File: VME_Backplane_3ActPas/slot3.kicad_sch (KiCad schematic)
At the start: 7 parts, among them X101 DIN41612_03x32_ABC_VMEbus, X402A1 Jumper_2_Open, X402B1 Jumper_2_Open, X402C1 Jumper_2_Open, X402D1 Jumper_2_Open, X502 Jumper_2_Open

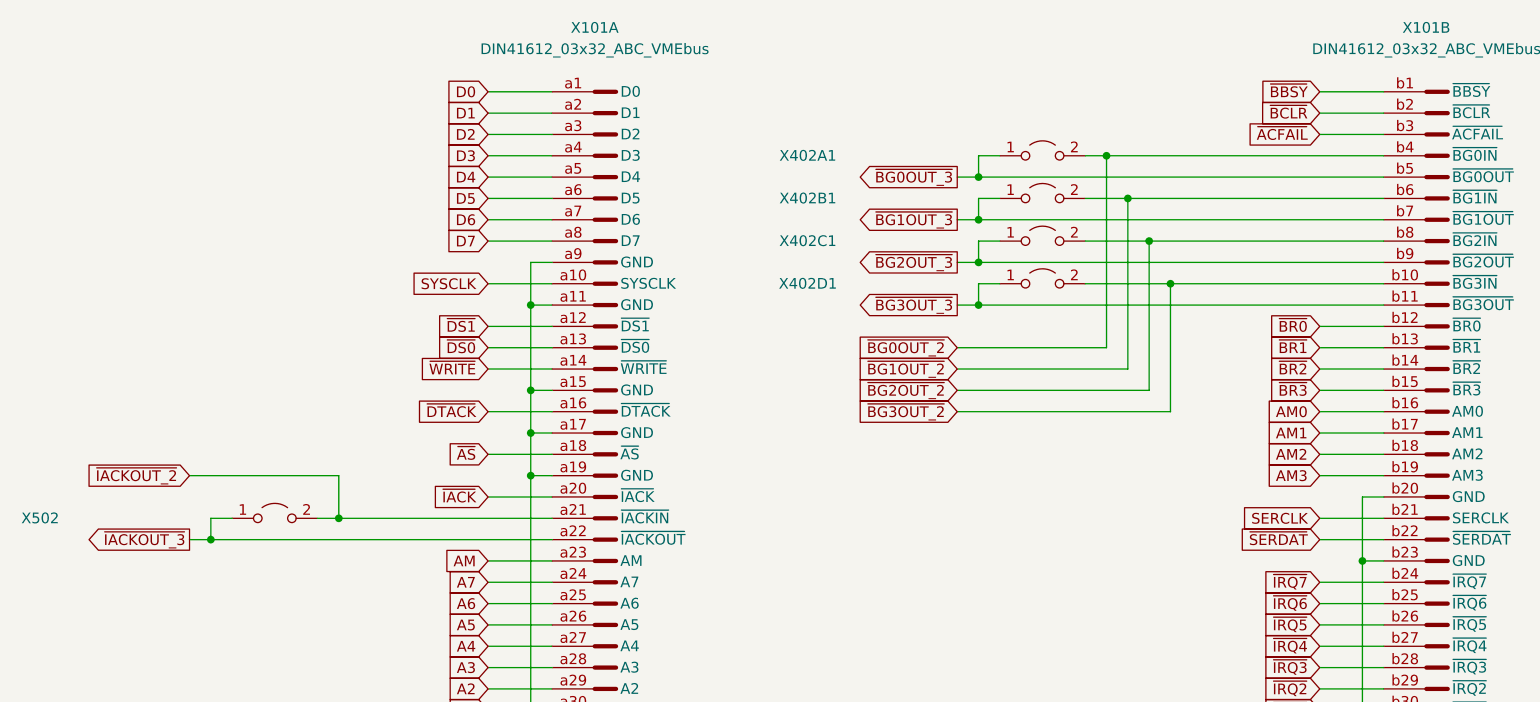
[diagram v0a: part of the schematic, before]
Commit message: Rename sheets to reflect their slots
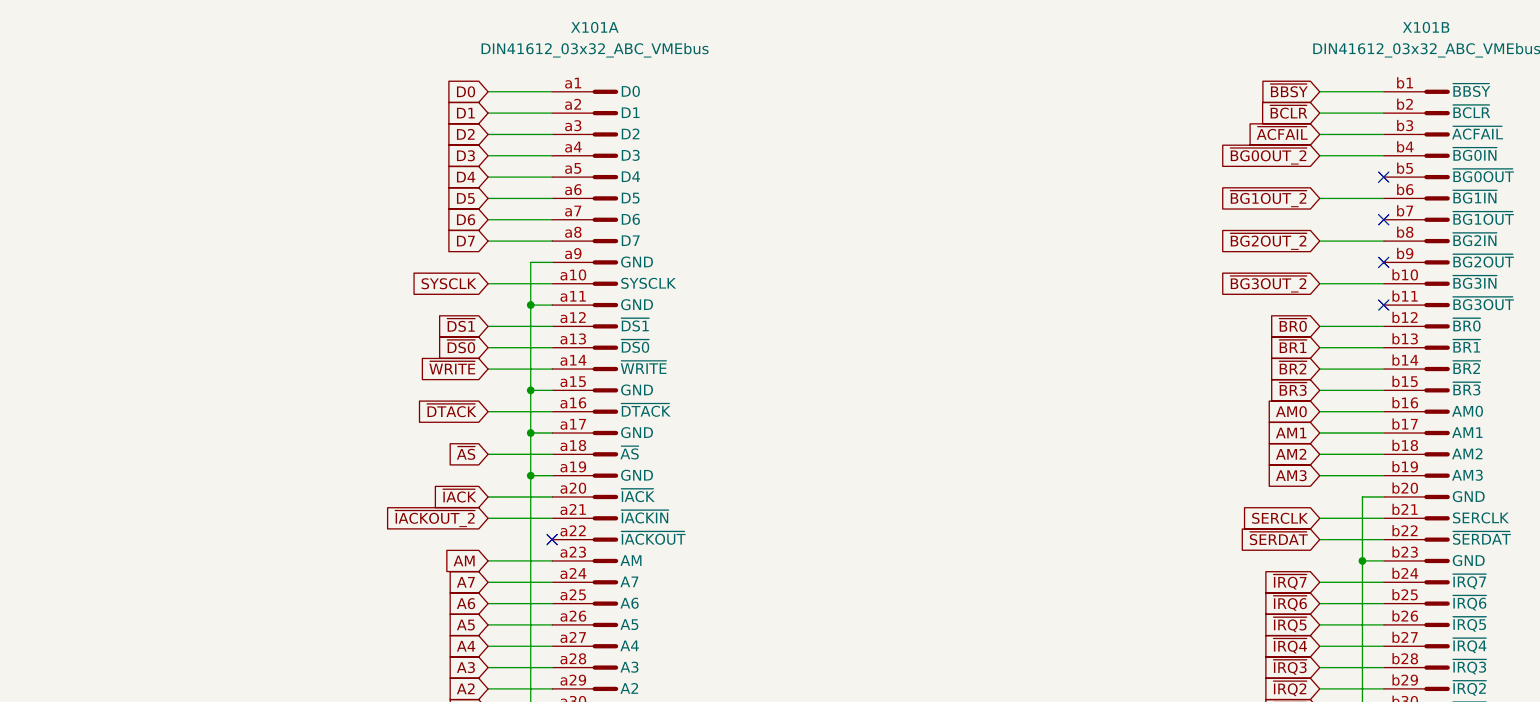
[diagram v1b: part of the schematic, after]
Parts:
- removed X402A1, X402B1, X402C1, X402D1, X502: Jumper_2_Open, Connector_PinHeader_2.54mm:PinHeader_1x02_P2.54mm_Vertical, symbol Jumper:Jumper_2_Open
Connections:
- net ~{BG0OUT_3}: no longer names the net of X101.b5 (~{BG0OUT})
- net ~{BG1OUT_3}: no longer names the net of X101.b7 (~{BG1OUT})
- net ~{BG2OUT_3}: no longer names the net of X101.b9 (~{BG2OUT})
- net ~{BG3OUT_3}: no longer names the net of X101.b11 (~{BG3OUT})
- net ~{IACKOUT_3}: no longer names the net of X101.a22 (~{IACKOUT})
- no-connect marks 0 -> 5
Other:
- title: SOCKET 1 -> SLOT 3

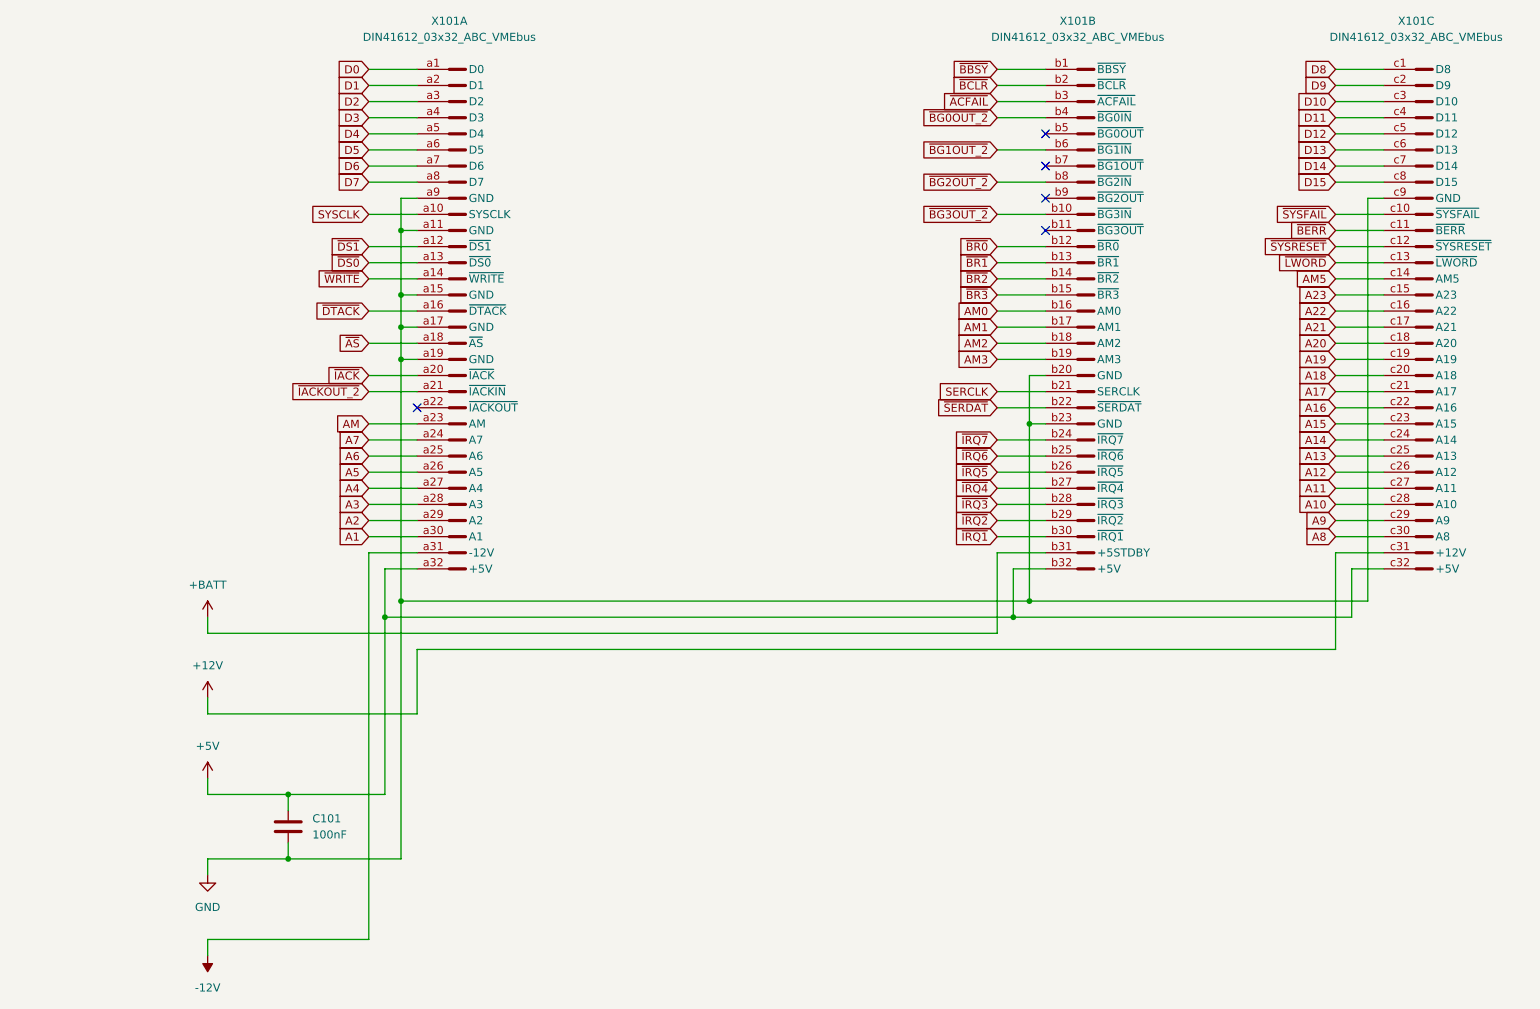
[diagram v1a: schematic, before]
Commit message: Change to own DIN 41612 footprint with 3D model
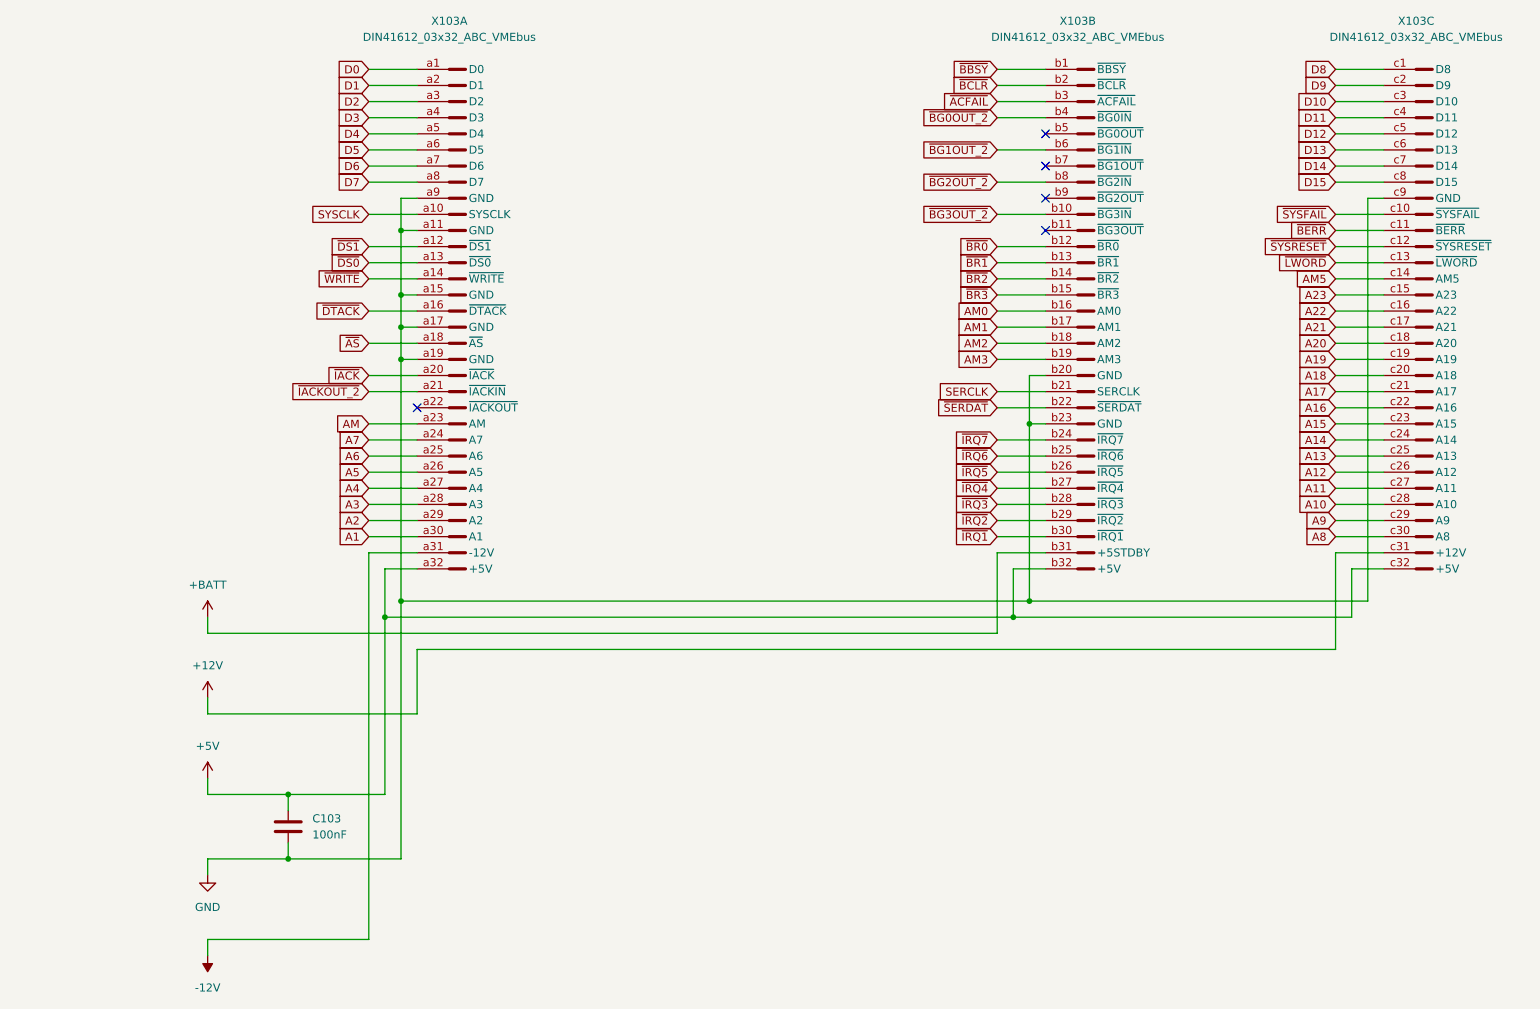
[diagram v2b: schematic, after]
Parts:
- X103: renamed from X101; footprint Connector_DIN:DIN41612_C_3x32_Female_Vertical_THT -> COMET footprints:Connector_DIN41612_C_3x32_Female_Vertical_THT
- X103: renamed from X101; footprint Connector_DIN:DIN41612_C_3x32_Male_Horizontal_THT -> COMET footprints:Connector_DIN41612_C_3x32_Female_Vertical_THT
- renumbered C101 to C103
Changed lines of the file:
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@@
   (symbol (lib_id "power:+5V") (at 55.88 149.86 0) (unit 1)
     (in_bom yes) (on_board yes) (fields_autoplaced)
-    (property "Reference" "#PWR?" (id 0) (at 55.88 153.67 0)
+    (property "Reference" "#PWR0133" (id 0) (at 55.88 153.67 0)
       (effects (font (size 1.27 1.27)) hide)
     )
@@
   (symbol (lib_id "COMET symbols:DIN41612_03x32_ABC_VMEbus") (at 93.98 76.2 0) (unit 1)
     (in_bom yes) (on_board yes)
-    (property "Reference" "X101" (id 0) (at 93.98 30.48 0))
+    (property "Reference" "X103" (id 0) (at 93.98 30.48 0))
     (property "Value" "DIN41612_03x32_ABC_VMEbus" (id 1) (at 93.98 33.02 0))
-    (property "Footprint" "Connector_DIN:DIN41612_C_3x32_Female_Vertical_THT" (id 2) (at 96.52 76.2 0)
+    (property "Footprint" "COMET footprints:Connector_DIN41612_C_3x32_Female_Vertical_THT" (id 2) (at 96.52 76.2 0)
       (effects (font (size 1.27 1.27)) hide)
     )
@@
   (symbol (lib_id "power:+12V") (at 55.88 137.16 0) (unit 1)
     (in_bom yes) (on_board yes) (fields_autoplaced)
-    (property "Reference" "#PWR?" (id 0) (at 55.88 140.97 0)
+    (property "Reference" "#PWR0134" (id 0) (at 55.88 140.97 0)
       (effects (font (size 1.27 1.27)) hide)
     )
@@
   (symbol (lib_id "COMET symbols:C") (at 68.58 157.48 0) (unit 1)
     (in_bom yes) (on_board yes) (fields_autoplaced)
-    (property "Reference" "C101" (id 0) (at 72.39 156.2099 0)
+    (property "Reference" "C103" (id 0) (at 72.39 156.2099 0)
       (effects (font (size 1.27 1.27)) (justify left))
     )
@@
   (symbol (lib_id "COMET symbols:DIN41612_03x32_ABC_VMEbus") (at 193.04 76.2 0) (unit 2)
     (in_bom yes) (on_board yes)
-    (property "Reference" "X101" (id 0) (at 193.04 30.48 0))
+    (property "Reference" "X103" (id 0) (at 193.04 30.48 0))
     (property "Value" "DIN41612_03x32_ABC_VMEbus" (id 1) (at 193.04 33.02 0))
-    (property "Footprint" "Connector_DIN:DIN41612_C_3x32_Male_Horizontal_THT" (id 2) (at 195.58 76.2 0)
+    (property "Footprint" "COMET footprints:Connector_DIN41612_C_3x32_Female_Vertical_THT" (id 2) (at 195.58 76.2 0)
       (effects (font (size 1.27 1.27)) hide)
     )
@@
   (symbol (lib_id "power:-12V") (at 55.88 177.8 180) (unit 1)
     (in_bom yes) (on_board yes) (fields_autoplaced)
-    (property "Reference" "#PWR?" (id 0) (at 55.88 180.34 0)
+    (property "Reference" "#PWR0132" (id 0) (at 55.88 180.34 0)
       (effects (font (size 1.27 1.27)) hide)
     )
@@
   (symbol (lib_id "COMET symbols:DIN41612_03x32_ABC_VMEbus") (at 246.38 76.2 0) (unit 3)
     (in_bom yes) (on_board yes)
-    (property "Reference" "X101" (id 0) (at 246.38 30.48 0))
+    (property "Reference" "X103" (id 0) (at 246.38 30.48 0))
     (property "Value" "DIN41612_03x32_ABC_VMEbus" (id 1) (at 246.38 33.02 0))
-    (property "Footprint" "Connector_DIN:DIN41612_C_3x32_Male_Horizontal_THT" (id 2) (at 248.92 76.2 0)
+    (property "Footprint" "COMET footprints:Connector_DIN41612_C_3x32_Female_Vertical_THT" (id 2) (at 248.92 76.2 0)
       (effects (font (size 1.27 1.27)) hide)
     )
@@
   (symbol (lib_id "power:+BATT") (at 55.88 124.46 0) (unit 1)
     (in_bom yes) (on_board yes) (fields_autoplaced)
-    (property "Reference" "#PWR?" (id 0) (at 55.88 128.27 0)
+    (property "Reference" "#PWR0135" (id 0) (at 55.88 128.27 0)
       (effects (font (size 1.27 1.27)) hide)
     )
@@
   (symbol (lib_id "power:GND") (at 55.88 165.1 0) (unit 1)
     (in_bom yes) (on_board yes) (fields_autoplaced)
-    (property "Reference" "#PWR?" (id 0) (at 55.88 171.45 0)
-      (effects (font (size 1.27 1.27)) hide)
-    )
+    (property "Reference" "#PWR0131" (id 0) (at 55.88 171.45 0)
+      (effects (font (size 1.27 1.27)) hide)
+    )

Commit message: Add/update revision information in schematics and PCB
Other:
- company: (C) TOM STOREY -> TOM STOREY
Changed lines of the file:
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@@
   (title_block
     (title "SLOT 3")
-    (date "2024-01-02")
+    (date "2024-01-03")
     (rev "1")
-    (company "(C) TOM STOREY")
+    (company "TOM STOREY")
     (comment 1 "FREE FOR NON-COMMERCIAL USE")
   )
